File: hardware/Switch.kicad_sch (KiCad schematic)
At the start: 54 parts, among them U11 ADG6412BCPZ, U14 ADG6412BCPZ, U17 ADG6412BCPZ, U2 PCAL6524HEAZ, U26 ADG6412BCPZ, U27 ADG6412BCPZ, U28 ADG6412BCPZ, U29 ADG6412BCPZ, U30 ADG6412BCPZ, U31 ADG6412BCPZ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

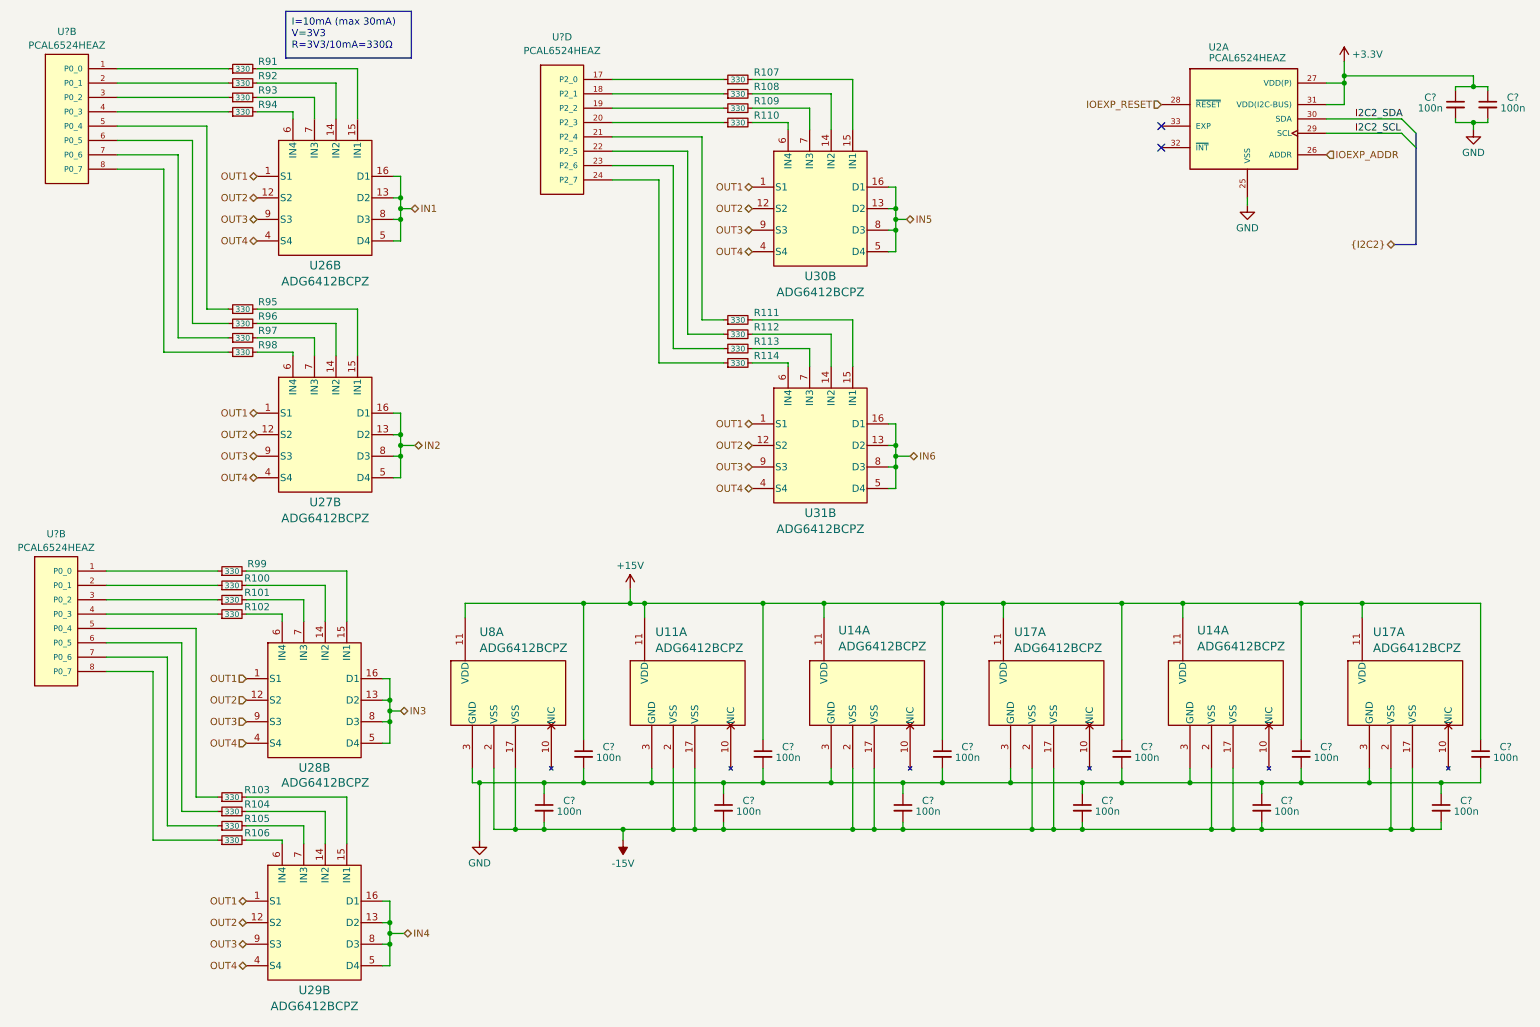
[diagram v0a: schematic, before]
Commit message: feat(RGB): WS2812B driver
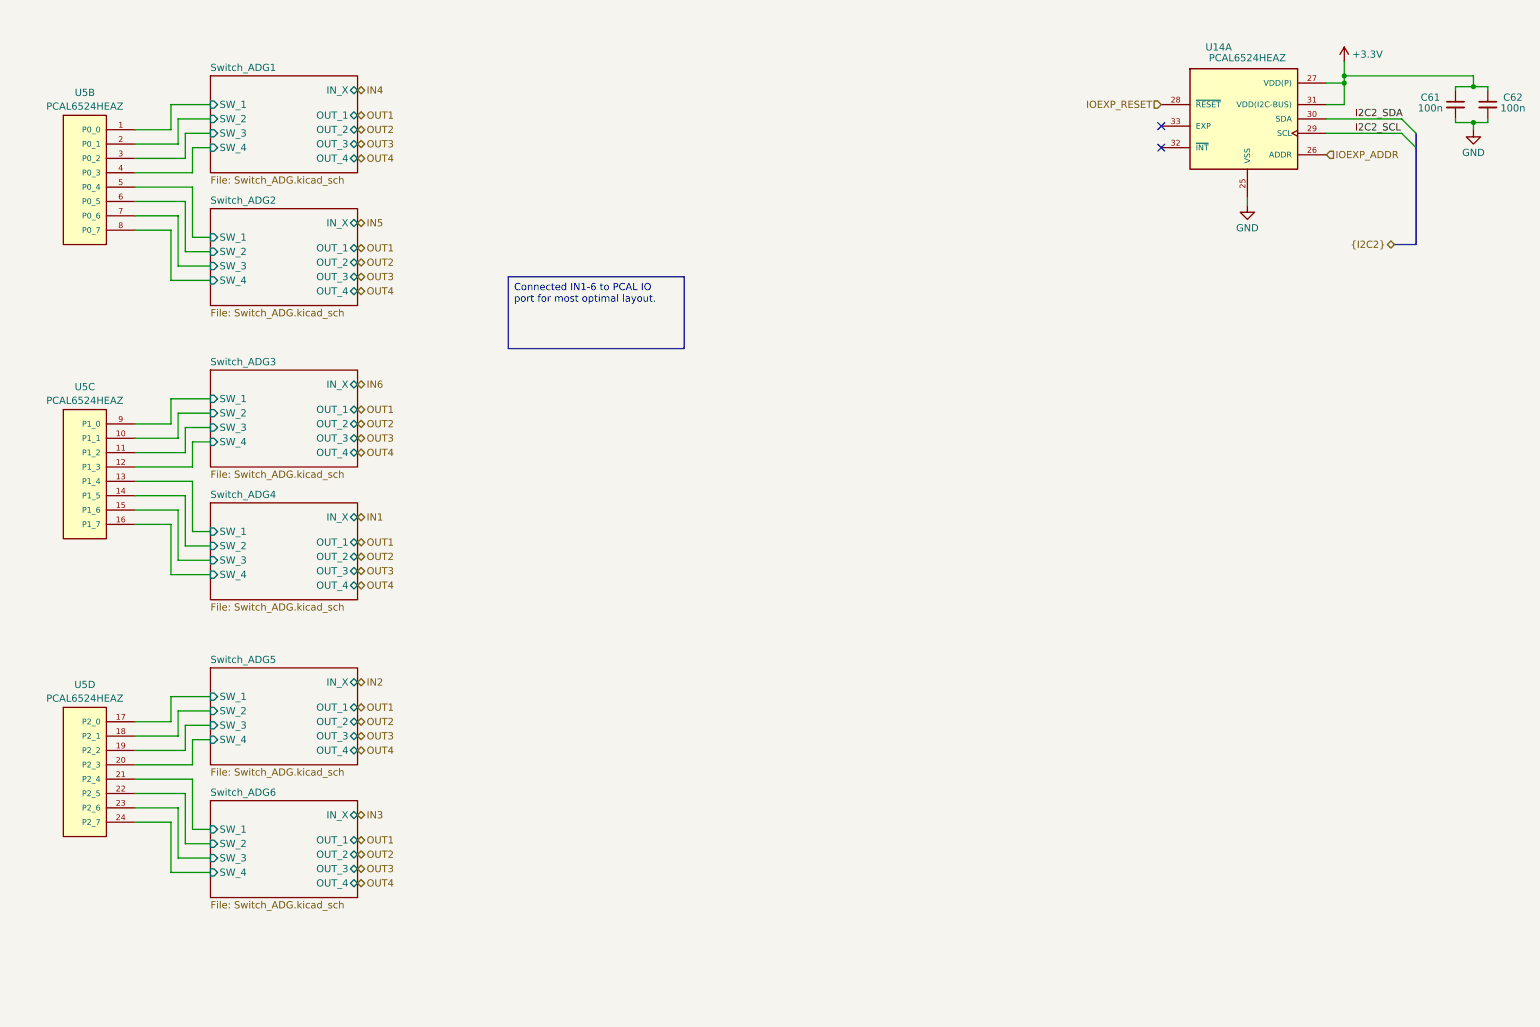
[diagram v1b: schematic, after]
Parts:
- removed C? (x12): 100n, Capacitor_SMD:C_0603_1608Metric, symbol Device:C_Small
- removed R100, R101, R102, R103, R104, R105, R106, R107, R108, R109, R110, R111, R112, R113, R114, R91, R92, R93, R94, R95, R96, R97, R98, R99: 330, Resistor_SMD:R_0603_1608Metric, symbol Device:R_Small
- removed U11, U14 (x2), U17 (x2), U26, U27, U28, U29, U30, U31, U8: ADG6412BCPZ, ADG6412BCPZ:ADG6412BCPZ, symbol ADG6412BCPZ:ADG6412BCPZ
- removed U? (x3): PCAL6524HEAZ, PCAL6524HE:PCAL6524HEAZ, symbol PCAL6524HE:PCAL6524HEAZ
- added U5: PCAL6524HEAZ, PCAL6524HE:PCAL6524HEAZ, symbol PCAL6524HE:PCAL6524HEAZ
- gave numbers to parts that had none: 2
- renumbered U2 to U14
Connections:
- new net Switch_ADG1/SW_1: U5.1 (P0_0)
- new net Switch_ADG1/SW_2: U5.2 (P0_1)
- new net Switch_ADG1/SW_3: U5.3 (P0_2)
- new net Switch_ADG1/SW_4: U5.4 (P0_3)
- new net Switch_ADG2/SW_1: U5.5 (P0_4)
- new net Switch_ADG2/SW_2: U5.6 (P0_5)
- new net Switch_ADG2/SW_3: U5.7 (P0_6)
- new net Switch_ADG2/SW_4: U5.8 (P0_7)
- new net Switch_ADG3/SW_1: U5.9 (P1_0)
- new net Switch_ADG3/SW_2: U5.10 (P1_1)
- new net Switch_ADG3/SW_3: U5.11 (P1_2)
- new net Switch_ADG3/SW_4: U5.12 (P1_3)
- new net Switch_ADG4/SW_1: U5.13 (P1_4)
- new net Switch_ADG4/SW_2: U5.14 (P1_5)
- new net Switch_ADG4/SW_3: U5.15 (P1_6)
- new net Switch_ADG4/SW_4: U5.16 (P1_7)
- new net Switch_ADG5/SW_1: U5.17 (P2_0)
- new net Switch_ADG5/SW_2: U5.18 (P2_1)
- new net Switch_ADG5/SW_3: U5.19 (P2_2)
- new net Switch_ADG5/SW_4: U5.20 (P2_3)
- new net Switch_ADG6/SW_1: U5.21 (P2_4)
- new net Switch_ADG6/SW_2: U5.22 (P2_5)
- new net Switch_ADG6/SW_3: U5.23 (P2_6)
- new net Switch_ADG6/SW_4: U5.24 (P2_7)
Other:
- added sheet Switch_ADG1 (Switch_ADG.kicad_sch)
- added sheet Switch_ADG2 (Switch_ADG.kicad_sch)
- added sheet Switch_ADG3 (Switch_ADG.kicad_sch)
- added sheet Switch_ADG4 (Switch_ADG.kicad_sch)
- added sheet Switch_ADG5 (Switch_ADG.kicad_sch)
- added sheet Switch_ADG6 (Switch_ADG.kicad_sch)

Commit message: HW: update to latest version
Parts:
- removed C61, C62: 100n, Capacitor_SMD:C_0603_1608Metric, symbol Device:C_Small
- removed U14, U5: PCAL6524HEAZ, PCAL6524HE:PCAL6524HEAZ, symbol PCAL6524HE:PCAL6524HEAZ
- added J1: Output connector, Phoenix Contact MSTBVA 2.5-4-G-5.08 - PCB header 1755752:1755752, symbol Connector_Generic:Conn_01x04
- added J5: Zoutwachter cable, Phoenix Contact MSTBVA 2.5-24-G-5.08 - PCB header 1755956:1755956, symbol Connector_Generic:Conn_01x24
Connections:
- new net FIELD_PIN1: J5.1 (Pin_1)
- new net FIELD_PIN10: J5.10 (Pin_10)
- new net FIELD_PIN11: J5.11 (Pin_11)
- new net FIELD_PIN12: J5.12 (Pin_12)
- new net FIELD_PIN13: J5.13 (Pin_13)
- new net FIELD_PIN14: J5.14 (Pin_14)
- new net FIELD_PIN15: J5.15 (Pin_15)
- new net FIELD_PIN16: J5.16 (Pin_16)
- new net FIELD_PIN17: J5.17 (Pin_17)
- new net FIELD_PIN18: J5.18 (Pin_18)
- new net FIELD_PIN19: J5.19 (Pin_19)
- new net FIELD_PIN2: J5.2 (Pin_2)
- new net FIELD_PIN20: J5.20 (Pin_20)
- new net FIELD_PIN21: J5.21 (Pin_21)
- new net FIELD_PIN22: J5.22 (Pin_22)
- new net FIELD_PIN23: J5.23 (Pin_23)
- new net FIELD_PIN24: J5.24 (Pin_24)
- new net FIELD_PIN3: J5.3 (Pin_3)
- new net FIELD_PIN4: J5.4 (Pin_4)
- new net FIELD_PIN5: J5.5 (Pin_5)
- new net FIELD_PIN6: J5.6 (Pin_6)
- new net FIELD_PIN7: J5.7 (Pin_7)
- new net FIELD_PIN8: J5.8 (Pin_8)
- new net FIELD_PIN9: J5.9 (Pin_9)
- new net SENSOR_PIN1: J1.1 (Pin_1)
- new net SENSOR_PIN2: J1.2 (Pin_2)
- new net SENSOR_PIN3: J1.3 (Pin_3)
- new net SENSOR_PIN4: J1.4 (Pin_4)
- no-connect marks 2 -> 0
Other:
- removed sheet Switch_ADG1
- removed sheet Switch_ADG2
- removed sheet Switch_ADG3
- removed sheet Switch_ADG4
- removed sheet Switch_ADG5
- removed sheet Switch_ADG6
- added sheet Switch Module 1 (Switch_Module.kicad_sch)
- added sheet Switch Module 2 (Switch_Module.kicad_sch)
- added sheet Switch Module 3 (Switch_Module.kicad_sch)
- added sheet Switch Module 4 (Switch_Module.kicad_sch)
- company: Avalution Engineering -> Avalution Engineering / Pollex
- title: Zoutwachter Switch -> Zoutwachter Measurement-Switch
